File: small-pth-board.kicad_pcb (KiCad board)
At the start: 2 copper layers, 80 x 60 mm, 3 parts, among them J1 POWER

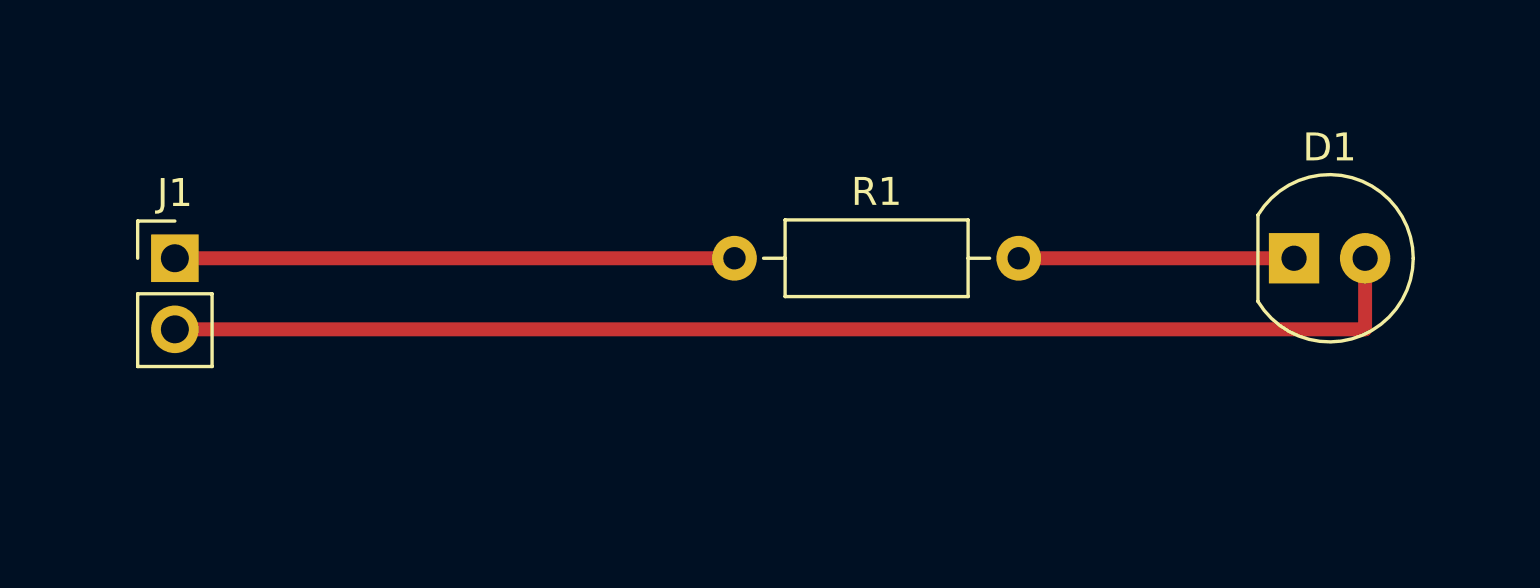
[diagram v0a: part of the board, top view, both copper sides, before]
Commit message: Fix LED polarity - cathode to GND, anode through resistor
Co-authored-by: markhu <239803+markhu@users.noreply.github.com>
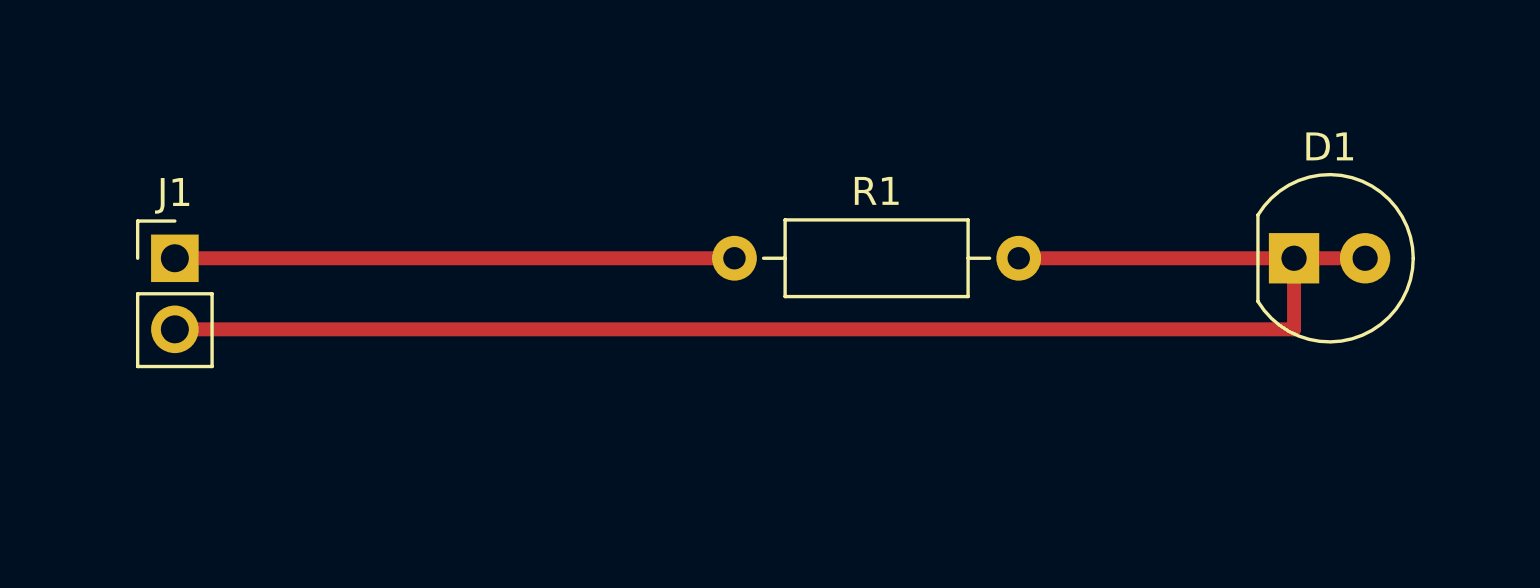
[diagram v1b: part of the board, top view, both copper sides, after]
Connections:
- D1 pad 1: Net-(D1-A) -> GND
- D1 pad 2: GND -> Net-(D1-A)
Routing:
- net Net-(D1-A): track 9.84 -> 12.4 mm
- net GND: track 45.1 -> 42.5 mm
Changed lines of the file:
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@@
     (fp_circle (center 1.27 0) (end 3.77 0) (layer "F.Fab") (stroke (width 0.1) (type solid)) (fill none))
     (pad "1" thru_hole rect (at 0 0) (size 1.8 1.8) (drill 0.9) (layers "*.Cu" "*.Mask")
-      (net 3 "Net-(D1-A)") (pinfunction "K") (pintype "passive"))
+      (net 2 "GND") (pinfunction "K") (pintype "passive"))
     (pad "2" thru_hole circle (at 2.54 0) (size 1.8 1.8) (drill 0.9) (layers "*.Cu" "*.Mask")
-      (net 2 "GND") (pinfunction "A") (pintype "passive"))
+      (net 3 "Net-(D1-A)") (pinfunction "A") (pintype "passive"))
     (model "${KICAD6_3DMODEL_DIR}/LED_THT.3dshapes/LED_D5.0mm.wrl"
       (offset (xyz 0 0 0))
@@
   )
   (segment (start 120 80) (end 140 80) (width 0.5) (layer "F.Cu") (net 1))
-  (segment (start 150.16 80) (end 160 80) (width 0.5) (layer "F.Cu") (net 3))
-  (segment (start 120 82.54) (end 162.54 82.54) (width 0.5) (layer "F.Cu") (net 2))
-  (segment (start 162.54 82.54) (end 162.54 80) (width 0.5) (layer "F.Cu") (net 2))
+  (segment (start 150.16 80) (end 162.54 80) (width 0.5) (layer "F.Cu") (net 3))
+  (segment (start 120 82.54) (end 160 82.54) (width 0.5) (layer "F.Cu") (net 2))
+  (segment (start 160 82.54) (end 160 80) (width 0.5) (layer "F.Cu") (net 2))
   (zone (net 2) (net_name "GND") (layer "F.Cu") (hatch edge 0.5)
     (connect_pads (clearance 0.5))
